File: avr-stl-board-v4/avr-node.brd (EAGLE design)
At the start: 67.2 x 86.4 mm, 36 parts, among them IC2 DS1307, IC3 LM358N, Q1 32.768kHz, Q3 16MHz, T1 S8050, U1 24LC256, U3 ATMEGA328P-PU

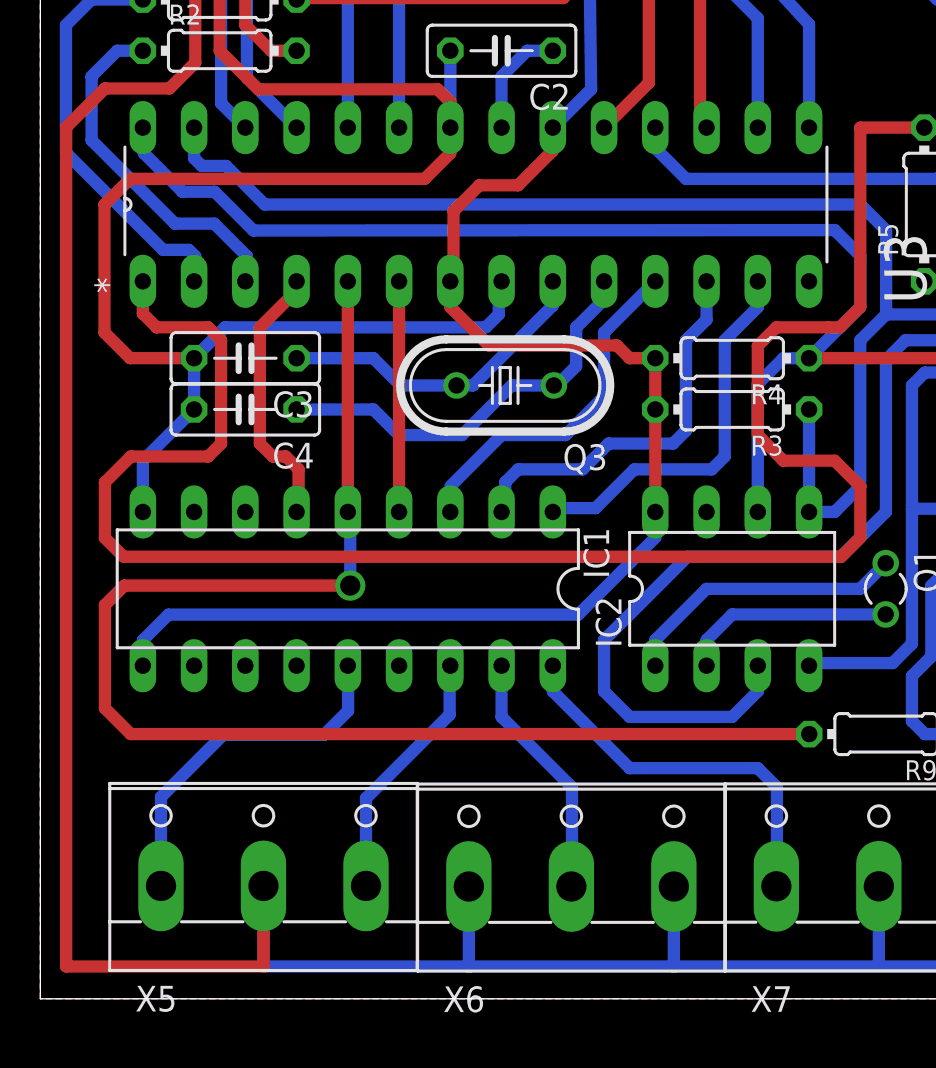
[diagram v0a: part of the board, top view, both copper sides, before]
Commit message: adding bit, byte, word persistant commands
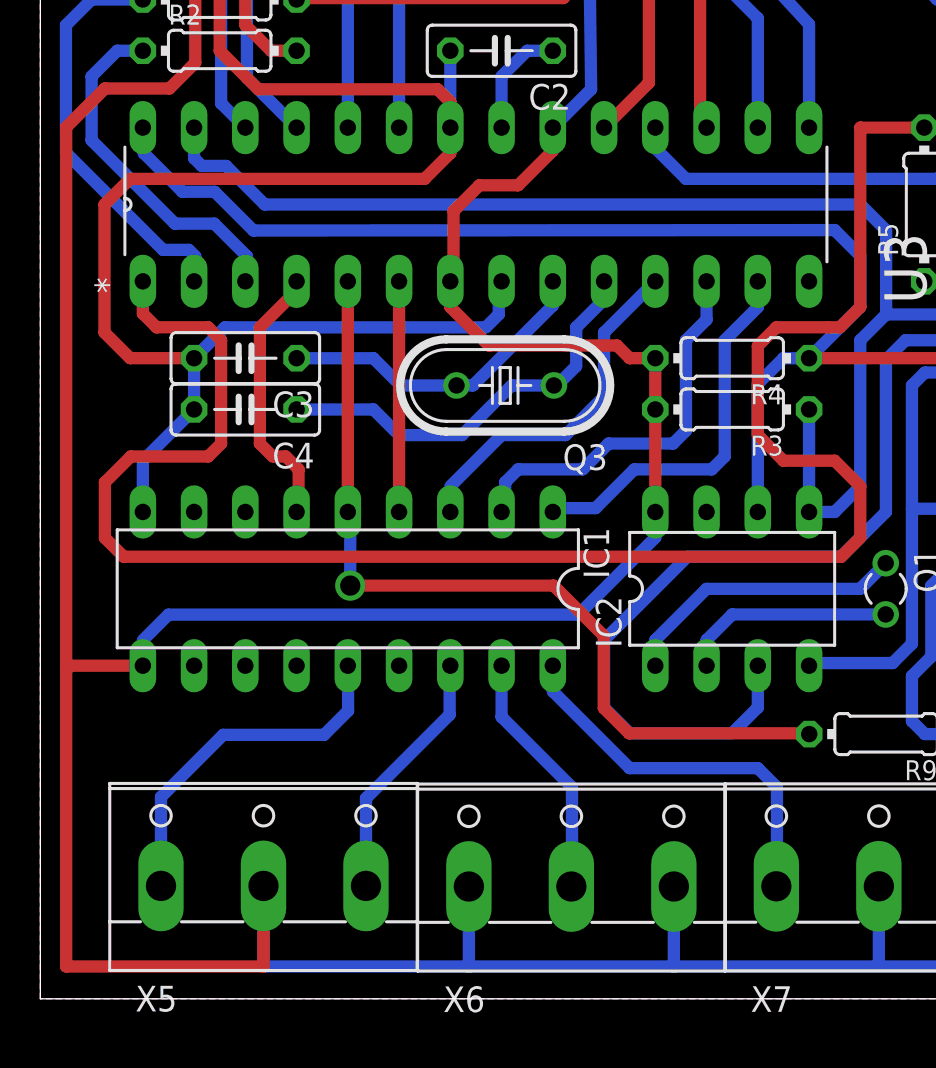
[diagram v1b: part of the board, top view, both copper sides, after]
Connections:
- net +5V: no longer IC1.10
- net V_IN: now also IC1.10
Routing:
- net AO1: track 68.2 -> 43.0 mm
- net V_IN: track 225.4 -> 229.3 mm
- net N$28: track 44.6 -> 46.2 mm
- net +5V: track 218.0 -> 216.7 mm
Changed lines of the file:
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@@
 <wire x1="6.4" y1="45.12" x2="3.2" y2="45.12" width="0.6096" layer="1"/>
 <wire x1="3.2" y1="45.12" x2="1.28" y2="43.2" width="0.6096" layer="1"/>
-<wire x1="1.28" y1="43.2" x2="1.28" y2="1.6" width="0.6096" layer="1"/>
+<wire x1="1.28" y1="43.2" x2="1.28" y2="16.298" width="0.6096" layer="1"/>
+<wire x1="1.28" y1="16.298" x2="1.28" y2="1.6" width="0.6096" layer="1"/>
 <wire x1="1.28" y1="1.6" x2="11.06" y2="1.6" width="0.6096" layer="1"/>
 <wire x1="11.06" y1="1.6" x2="11.06" y2="5.595" width="0.6096" layer="1"/>
@@
 <wire x1="15.68" y1="65.92" x2="5.8" y2="65.92" width="0.6096" layer="1"/>
 <wire x1="5.8" y1="65.92" x2="5.48" y2="66.24" width="0.6096" layer="1"/>
+<contactref element="IC1" pad="10"/>
+<wire x1="5.08" y1="16.51" x2="1.492" y2="16.51" width="0.6096" layer="1"/>
+<wire x1="1.492" y1="16.51" x2="1.28" y2="16.298" width="0.6096" layer="1"/>
 </signal>
 <signal name="+5V">
@@
 <contactref element="U1" pad="8"/>
 <contactref element="IC2" pad="8"/>
-<contactref element="IC1" pad="10"/>
-<wire x1="5.08" y1="16.51" x2="5.08" y2="17.77" width="0.6096" layer="16"/>
 <wire x1="5.08" y1="17.77" x2="6.35" y2="19.04" width="0.6096" layer="16"/>
 <wire x1="6.35" y1="19.04" x2="26.66" y2="19.04" width="0.6096" layer="16"/>
@@
 <contactref element="U3" pad="5"/>
 <contactref element="R9" pad="2"/>
-<wire x1="38.11" y1="13.12" x2="4.48" y2="13.12" width="0.6096" layer="1"/>
-<wire x1="4.48" y1="13.12" x2="3.2" y2="14.4" width="0.6096" layer="1"/>
-<wire x1="3.2" y1="14.4" x2="3.2" y2="19.52" width="0.6096" layer="1"/>
-<wire x1="3.2" y1="19.52" x2="4.16" y2="20.48" width="0.6096" layer="1"/>
 <contactref element="IC1" pad="5"/>
-<wire x1="4.16" y1="20.48" x2="15.36" y2="20.48" width="0.6096" layer="1"/>
 <via x="15.36" y="20.48" extent="1-16" drill="1"/>
 <wire x1="15.36" y1="20.48" x2="15.36" y2="23.93" width="0.6096" layer="16"/>
 <wire x1="15.36" y1="23.93" x2="15.24" y2="24.13" width="0.6096" layer="16"/>
 <wire x1="15.24" y1="35.56" x2="15.24" y2="24.13" width="0.6096" layer="1"/>
+<wire x1="15.36" y1="20.48" x2="25.439" y2="20.48" width="0.6096" layer="1"/>
+<wire x1="25.439" y1="20.48" x2="27.924" y2="17.995" width="0.6096" layer="1"/>
+<wire x1="27.924" y1="17.995" x2="27.924" y2="14.414" width="0.6096" layer="1"/>
+<wire x1="27.924" y1="14.414" x2="29.181" y2="13.157" width="0.6096" layer="1"/>
+<wire x1="38.073" y1="13.157" x2="29.181" y2="13.157" width="0.6096" layer="1"/>
+<wire x1="38.073" y1="13.157" x2="38.11" y2="13.12" width="0" layer="19" extent="1-1"/>
 </signal>
 <signal name="AO2">
@@
 <contactref element="G1" pad="P$2"/>
 <contactref element="IC2" pad="3"/>
-<wire x1="35.56" y1="16.51" x2="35.56" y2="15.24" width="0.6096" layer="16"/>
-<wire x1="35.56" y1="15.24" x2="34.29" y2="13.97" width="0.6096" layer="16"/>
-<wire x1="34.29" y1="13.97" x2="29.21" y2="13.97" width="0.6096" layer="16"/>
-<wire x1="29.21" y1="13.97" x2="27.94" y2="15.24" width="0.6096" layer="16"/>
-<wire x1="27.94" y1="15.24" x2="27.94" y2="17.78" width="0.6096" layer="16"/>
+<wire x1="35.56" y1="16.51" x2="35.56" y2="14.434" width="0.6096" layer="16"/>
+<wire x1="35.56" y1="14.434" x2="34.29" y2="13.164" width="0.6096" layer="16"/>
+<wire x1="34.29" y1="13.164" x2="29.21" y2="13.164" width="0.6096" layer="16"/>
+<wire x1="29.21" y1="13.164" x2="27.94" y2="14.434" width="0.6096" layer="16"/>
+<wire x1="27.94" y1="14.434" x2="27.94" y2="17.78" width="0.6096" layer="16"/>
 <wire x1="27.94" y1="17.78" x2="32.07" y2="21.91" width="0.6096" layer="16"/>
 <wire x1="32.07" y1="21.91" x2="39.69" y2="21.91" width="0.6096" layer="16"/>
